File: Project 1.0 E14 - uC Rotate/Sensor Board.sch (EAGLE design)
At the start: 95 parts, among them IC1 LT1963EST-1.5, IC2 LT1963EST-1.5, IC4 LT1963EST-1.5

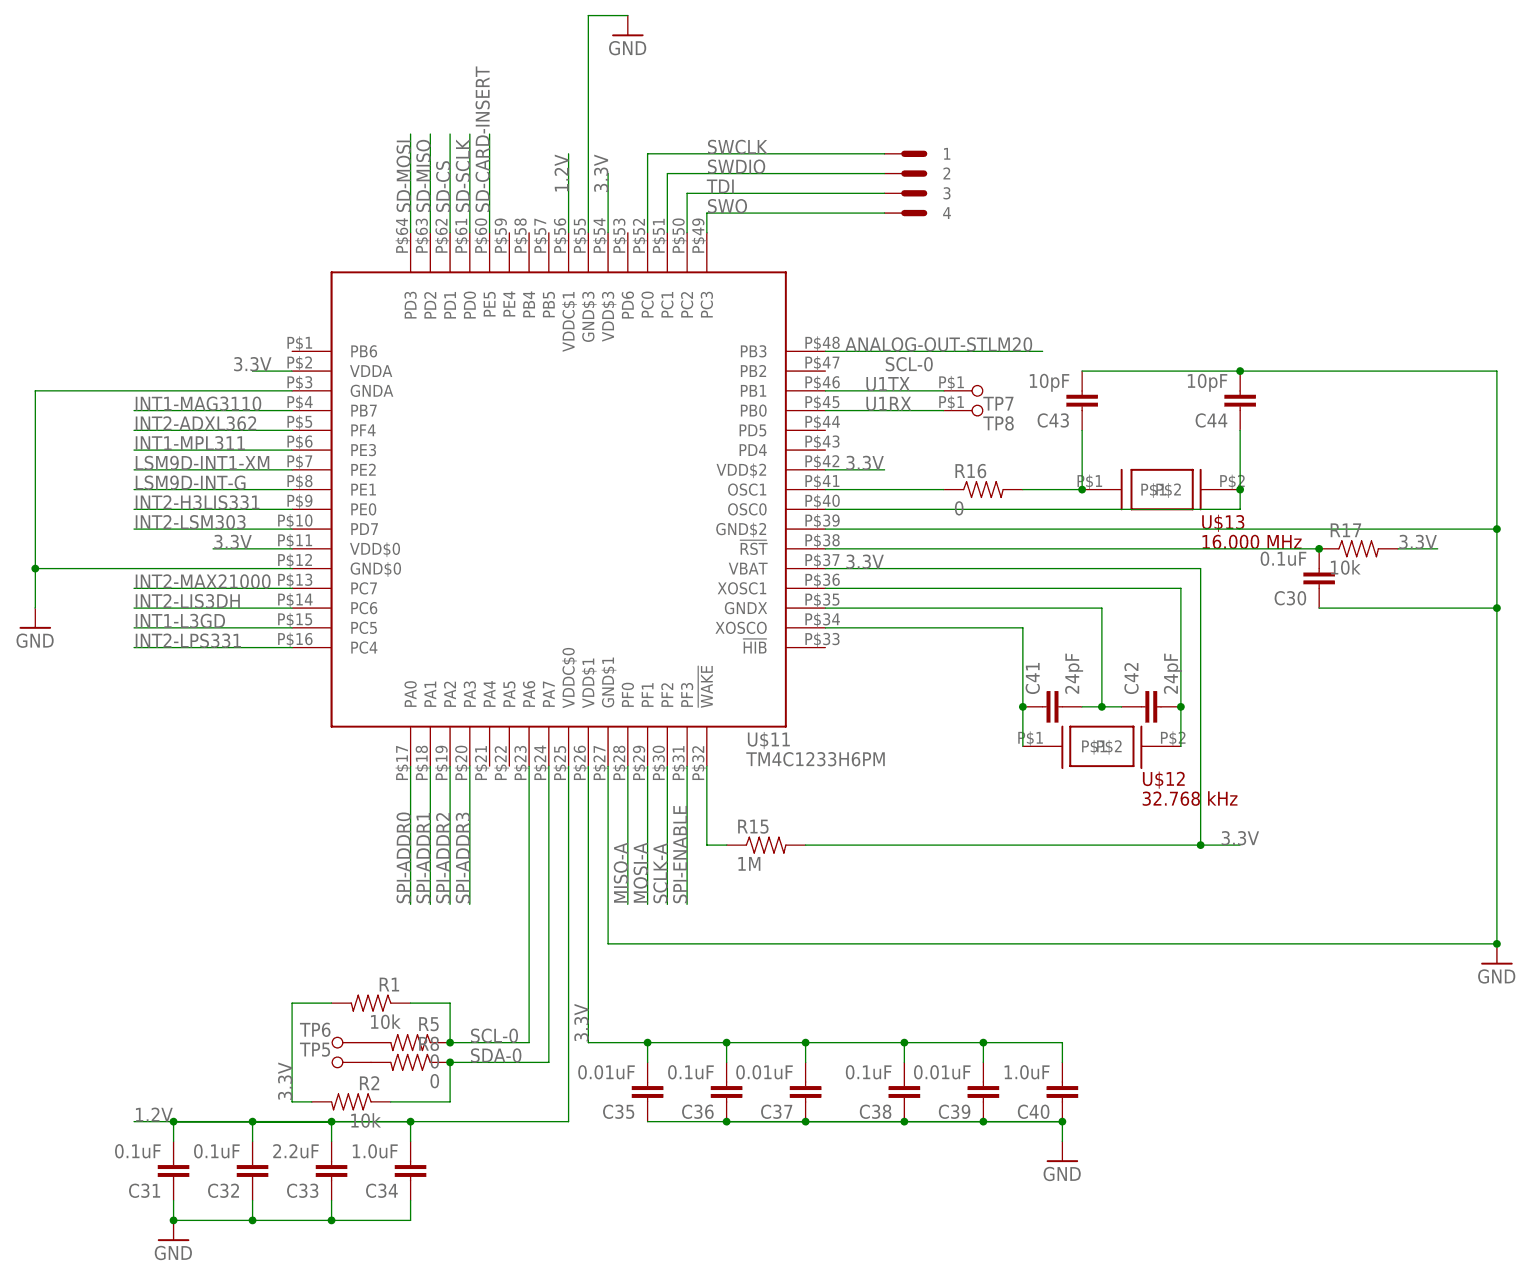
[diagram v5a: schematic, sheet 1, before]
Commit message: Sensor Test Board: Corrected LSM9D0 interrupt issue by adding int2-XM and removing int1_G and replacing it with DRDY_G. Some 3.3v traces have been connected but these wil need to be checked to ensure the LDO is not overloaded.
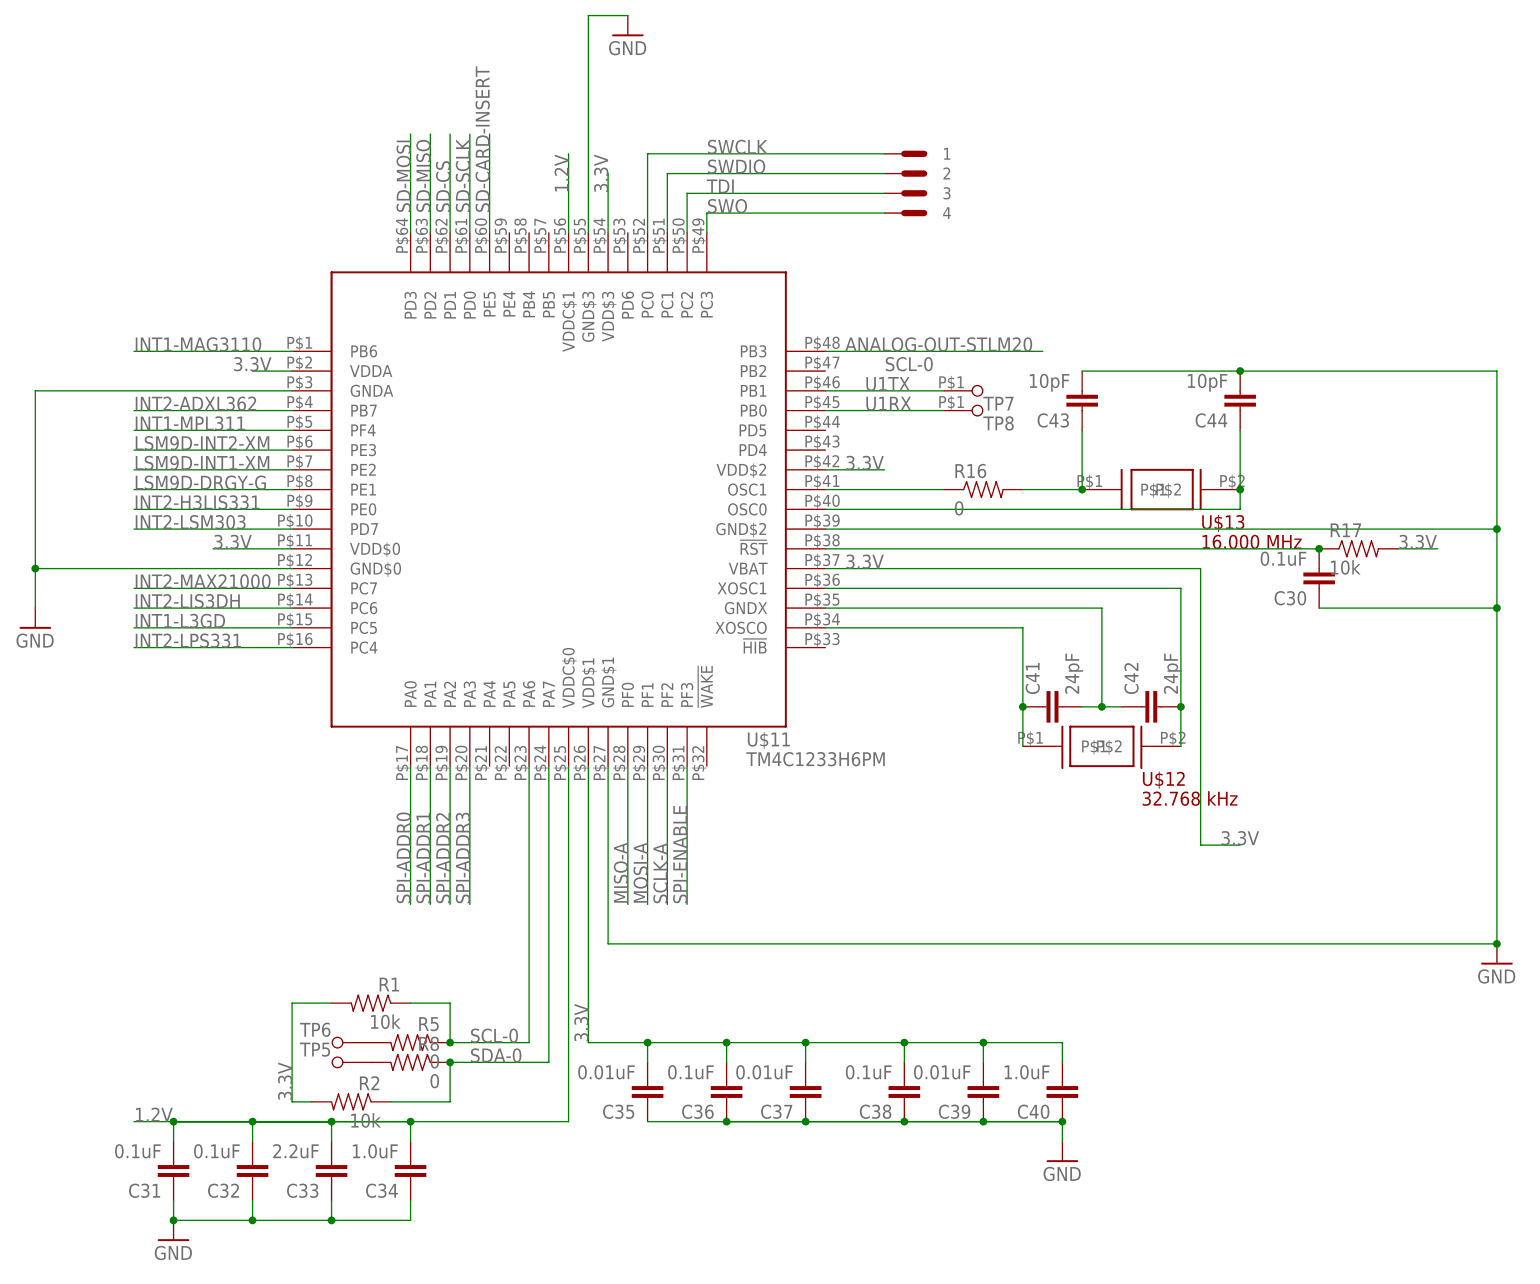
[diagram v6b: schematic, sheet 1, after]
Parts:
- removed R15: 1M, Kas-Passives:RESISTOR
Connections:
- removed net N$18: R15.1, U$11.!WAKE
- new net LSM9D-INT2-XM: U$11.PE3, U$17.INT2_XM
- net 3.3V: no longer R15.2
- net INT1-MAG3110: now also U$11.PB6; no longer U$11.PB7
- net INT1-MPL311: now also U$11.PF4; no longer U$11.PE3
- net INT2-ADXL362: now also U$11.PB7; no longer U$11.PF4
- net LSM9D-DRGY-G: now also U$11.PE1
- net LSM9D-INT-G: no longer U$11.PE1
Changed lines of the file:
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@@
 <part name="GND31" library="SparkFun-Aesthetics" deviceset="GND" device=""/>
 <part name="GND32" library="SparkFun-Aesthetics" deviceset="GND" device=""/>
-<part name="R15" library="Kas-Passives" deviceset="RESISTOR" device="" value="1M"/>
 <part name="C30" library="Kas-Passives" deviceset="CAPACITOR" device="" value="0.1uF"/>
 <part name="C31" library="Kas-Passives" deviceset="CAPACITOR" device="" value="0.1uF"/>
@@
 <instance part="GND31" gate="1" x="10.16" y="58.42"/>
 <instance part="GND32" gate="1" x="121.92" y="-60.96"/>
-<instance part="R15" gate="G$1" x="27.94" y="-45.72"/>
 <instance part="C30" gate="G$1" x="99.06" y="-10.16" rot="R180"/>
 <instance part="C31" gate="G$1" x="-48.26" y="-86.36" rot="R180"/>
@@
 </segment>
 </net>
-<net name="N$18" class="0">
-<segment>
-<pinref part="U$11" gate="G$1" pin="!WAKE"/>
-<wire x1="20.32" y1="-35.56" x2="20.32" y2="-45.72" width="0.1524" layer="91"/>
-<pinref part="R15" gate="G$1" pin="1"/>
-<wire x1="20.32" y1="-45.72" x2="22.86" y2="-45.72" width="0.1524" layer="91"/>
-</segment>
-</net>
 <net name="3.3V" class="0">
 <segment>
@@
 <pinref part="U$11" gate="G$1" pin="VBAT"/>
 <wire x1="83.82" y1="-10.16" x2="35.56" y2="-10.16" width="0.1524" layer="91"/>
-<pinref part="R15" gate="G$1" pin="2"/>
-<wire x1="33.02" y1="-45.72" x2="83.82" y2="-45.72" width="0.1524" layer="91"/>
 <wire x1="83.82" y1="-10.16" x2="83.82" y2="-45.72" width="0.1524" layer="91"/>
 <wire x1="83.82" y1="-45.72" x2="88.9" y2="-45.72" width="0.1524" layer="91"/>
-<junction x="83.82" y="-45.72"/>
 <label x="38.1" y="-10.16" size="1.778" layer="95"/>
 <label x="86.36" y="-45.72" size="1.778" layer="95"/>
@@
 </segment>
 </net>
-<net name="LSM9D-INT-G" class="0">
+<net name="INT1-MAG3110" class="0">
+<segment>
+<label x="-53.34" y="17.78" size="1.778" layer="95"/>
+<pinref part="U$11" gate="G$1" pin="PB6"/>
+<wire x1="-53.34" y1="17.78" x2="-33.02" y2="17.78" width="0.1524" layer="91"/>
+</segment>
+</net>
+<net name="INT1-L3GD" class="0">
+<segment>
+<pinref part="U$11" gate="G$1" pin="PC5"/>
+<wire x1="-53.34" y1="-17.78" x2="-33.02" y2="-17.78" width="0.1524" layer="91"/>
+<label x="-53.34" y="-17.78" size="1.778" layer="95"/>
+</segment>
+</net>
+<net name="INT2-MAX21000" class="0">
+<segment>
+<label x="-53.34" y="-12.7" size="1.778" layer="95"/>
+<pinref part="U$11" gate="G$1" pin="PC7"/>
+<wire x1="-53.34" y1="-12.7" x2="-33.02" y2="-12.7" width="0.1524" layer="91"/>
+</segment>
+</net>
+<net name="INT2-LPS331" class="0">
+<segment>
+<pinref part="U$11" gate="G$1" pin="PC4"/>
+<wire x1="-53.34" y1="-20.32" x2="-33.02" y2="-20.32" width="0.1524" layer="91"/>
+<label x="-53.34" y="-20.32" size="1.778" layer="95"/>
+</segment>
+</net>
+<net name="INT1-MPL311" class="0">
+<segment>
+<label x="-53.34" y="7.62" size="1.778" layer="95"/>
+<pinref part="U$11" gate="G$1" pin="PF4"/>
+<wire x1="-53.34" y1="7.62" x2="-33.02" y2="7.62" width="0.1524" layer="91"/>
+</segment>
+</net>
+<net name="INT2-LSM303" class="0">
+<segment>
+<label x="-53.34" y="-5.08" size="1.778" layer="95"/>
+<pinref part="U$11" gate="G$1" pin="PD7"/>
+<wire x1="-53.34" y1="-5.08" x2="-33.02" y2="-5.08" width="0.1524" layer="91"/>
+</segment>
+</net>
+<net name="INT2-LIS3DH" class="0">
+<segment>
+<pinref part="U$11" gate="G$1" pin="PC6"/>
+<wire x1="-33.02" y1="-15.24" x2="-53.34" y2="-15.24" width="0.1524" layer="91"/>
+<label x="-53.34" y="-15.24" size="1.778" layer="95"/>
+</segment>
+</net>
+<net name="INT2-ADXL362" class="0">
+<segment>
+<label x="-53.34" y="10.16" size="1.778" layer="95"/>
+<pinref part="U$11" gate="G$1" pin="PB7"/>
+<wire x1="-53.34" y1="10.16" x2="-33.02" y2="10.16" width="0.1524" layer="91"/>
+</segment>
+</net>
+<net name="INT2-H3LIS331" class="0">
+<segment>
+<label x="-53.34" y="-2.54" size="1.778" layer="95"/>
+<pinref part="U$11" gate="G$1" pin="PE0"/>
+<wire x1="-53.34" y1="-2.54" x2="-33.02" y2="-2.54" width="0.1524" layer="91"/>
+</segment>
+</net>
+<net name="SPI-ADDR3" class="0">
+<segment>
+<label x="-10.16" y="-53.34" size="1.778" layer="95" rot="R90"/>
+<pinref part="U$11" gate="G$1" pin="PA3"/>
+<wire x1="-10.16" y1="-53.34" x2="-10.16" y2="-35.56" width="0.1524" layer="91"/>
+</segment>
+</net>
+<net name="SPI-ADDR2" class="0">
+<segment>
+<label x="-12.7" y="-53.34" size="1.778" layer="95" rot="R90"/>
+<pinref part="U$11" gate="G$1" pin="PA2"/>
+<wire x1="-12.7" y1="-53.34" x2="-12.7" y2="-35.56" width="0.1524" layer="91"/>
+</segment>
+</net>
+<net name="SPI-ADDR1" class="0">
+<segment>
+<label x="-15.24" y="-53.34" size="1.778" layer="95" rot="R90"/>
+<pinref part="U$11" gate="G$1" pin="PA1"/>
+<wire x1="-15.24" y1="-53.34" x2="-15.24" y2="-35.56" width="0.1524" layer="91"/>
+</segment>
+</net>
+<net name="N$24" class="0">
+<segment>
+<pinref part="TP6" gate="G$1" pin="P$1"/>
+<pinref part="R5" gate="G$1" pin="2"/>
+</segment>
+</net>
+<net name="N$26" class="0">
+<segment>
+<pinref part="TP5" gate="G$1" pin="P$1"/>
+<pinref part="R8" gate="G$1" pin="2"/>
+</segment>
+</net>
+<net name="LSM9D-DRGY-G" class="0">
 <segment>
 <label x="-53.34" y="0" size="1.778" layer="95"/>
@@
 </segment>
 </net>
-<net name="INT1-MAG3110" class="0">
-<segment>
-<label x="-53.34" y="10.16" size="1.778" layer="95"/>
-<pinref part="U$11" gate="G$1" pin="PB7"/>
-<wire x1="-53.34" y1="10.16" x2="-33.02" y2="10.16" width="0.1524" layer="91"/>
-</segment>
-</net>
-<net name="INT1-L3GD" class="0">
-<segment>
-<pinref part="U$11" gate="G$1" pin="PC5"/>
-<wire x1="-53.34" y1="-17.78" x2="-33.02" y2="-17.78" width="0.1524" layer="91"/>
-<label x="-53.34" y="-17.78" size="1.778" layer="95"/>
-</segment>
-</net>
-<net name="INT2-MAX21000" class="0">
-<segment>
-<label x="-53.34" y="-12.7" size="1.778" layer="95"/>
-<pinref part="U$11" gate="G$1" pin="PC7"/>
-<wire x1="-53.34" y1="-12.7" x2="-33.02" y2="-12.7" width="0.1524" layer="91"/>
-</segment>
-</net>
-<net name="INT2-LPS331" class="0">
-<segment>
-<pinref part="U$11" gate="G$1" pin="PC4"/>
-<wire x1="-53.34" y1="-20.32" x2="-33.02" y2="-20.32" width="0.1524" layer="91"/>
-<label x="-53.34" y="-20.32" size="1.778" layer="95"/>
-</segment>
-</net>
-<net name="INT1-MPL311" class="0">
-<segment>
+<net name="LSM9D-INT2-XM" class="0">
+<segment>
+<pinref part="U$11" gate="G$1" pin="PE3"/>
+<wire x1="-33.02" y1="5.08" x2="-53.34" y2="5.08" width="0.1524" layer="91"/>
 <label x="-53.34" y="5.08" size="1.778" layer="95"/>
-<pinref part="U$11" gate="G$1" pin="PE3"/>
-<wire x1="-53.34" y1="5.08" x2="-33.02" y2="5.08" width="0.1524" layer="91"/>
-</segment>
-</net>
-<net name="INT2-LSM303" class="0">
-<segment>
-<label x="-53.34" y="-5.08" size="1.778" layer="95"/>
-<pinref part="U$11" gate="G$1" pin="PD7"/>
-<wire x1="-53.34" y1="-5.08" x2="-33.02" y2="-5.08" width="0.1524" layer="91"/>
-</segment>
-</net>
-<net name="INT2-LIS3DH" class="0">
-<segment>
-<pinref part="U$11" gate="G$1" pin="PC6"/>
-<wire x1="-33.02" y1="-15.24" x2="-53.34" y2="-15.24" width="0.1524" layer="91"/>
-<label x="-53.34" y="-15.24" size="1.778" layer="95"/>
-</segment>
-</net>
-<net name="INT2-ADXL362" class="0">
-<segment>
-<label x="-53.34" y="7.62" size="1.778" layer="95"/>
-<pinref part="U$11" gate="G$1" pin="PF4"/>
-<wire x1="-53.34" y1="7.62" x2="-33.02" y2="7.62" width="0.1524" layer="91"/>
-</segment>
-</net>
-<net name="INT2-H3LIS331" class="0">
-<segment>
-<label x="-53.34" y="-2.54" size="1.778" layer="95"/>
-<pinref part="U$11" gate="G$1" pin="PE0"/>
-<wire x1="-53.34" y1="-2.54" x2="-33.02" y2="-2.54" width="0.1524" layer="91"/>
-</segment>
-</net>
-<net name="SPI-ADDR3" class="0">
-<segment>
-<label x="-10.16" y="-53.34" size="1.778" layer="95" rot="R90"/>
-<pinref part="U$11" gate="G$1" pin="PA3"/>
-<wire x1="-10.16" y1="-53.34" x2="-10.16" y2="-35.56" width="0.1524" layer="91"/>
-</segment>
-</net>
-<net name="SPI-ADDR2" class="0">
-<segment>
-<label x="-12.7" y="-53.34" size="1.778" layer="95" rot="R90"/>
-<pinref part="U$11" gate="G$1" pin="PA2"/>
-<wire x1="-12.7" y1="-53.34" x2="-12.7" y2="-35.56" width="0.1524" layer="91"/>
-</segment>
-</net>
-<net name="SPI-ADDR1" class="0">
-<segment>
-<label x="-15.24" y="-53.34" size="1.778" layer="95" rot="R90"/>
-<pinref part="U$11" gate="G$1" pin="PA1"/>
-<wire x1="-15.24" y1="-53.34" x2="-15.24" y2="-35.56" width="0.1524" layer="91"/>
-</segment>
-</net>
-<net name="N$24" class="0">
-<segment>
-<pinref part="TP6" gate="G$1" pin="P$1"/>
-<pinref part="R5" gate="G$1" pin="2"/>
-</segment>
-</net>
-<net name="N$26" class="0">
-<segment>
-<pinref part="TP5" gate="G$1" pin="P$1"/>
-<pinref part="R8" gate="G$1" pin="2"/>
 </segment>
 </net>
@@
 </segment>
 </net>
+<net name="LSM9D-INT2-XM" class="0">
+<segment>
+<pinref part="U$17" gate="G$1" pin="INT2_XM"/>
+<wire x1="20.32" y1="-5.08" x2="35.56" y2="-5.08" width="0.1524" layer="91"/>
+<label x="22.86" y="-5.08" size="1.778" layer="95"/>
+</segment>
+</net>

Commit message: Sensor Test Board: Added library component (Atmel Tem sensor) and named one net so that it reflected its function and connected as needed (3.3V)
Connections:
- removed net LSM9D-INT-G: U$17.INT_G
- removed net N$25: C15.1, C16.1, U$5.VDD
- net 3.3V: now also C15.1, C16.1, U$5.VDD
